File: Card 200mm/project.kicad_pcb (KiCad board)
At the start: 2 copper layers, 51.5 x 22 mm, 8 parts, among them J1 Conn_01x04, J2 Conn_01x10, J3 Conn_01x10, J4 Conn_01x10, J5 Conn_01x10, U1 24LC32, X0 Card Edge

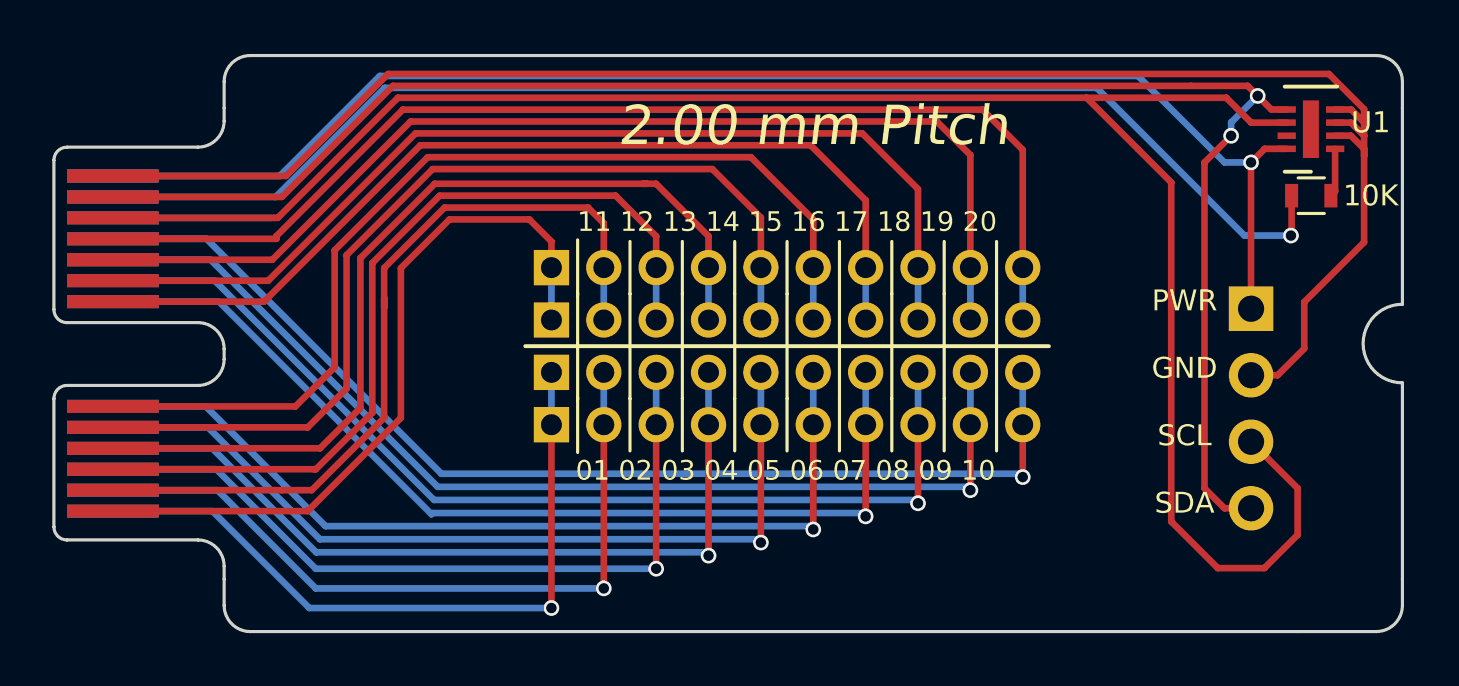
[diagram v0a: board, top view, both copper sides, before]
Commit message: EEPROM footprint update
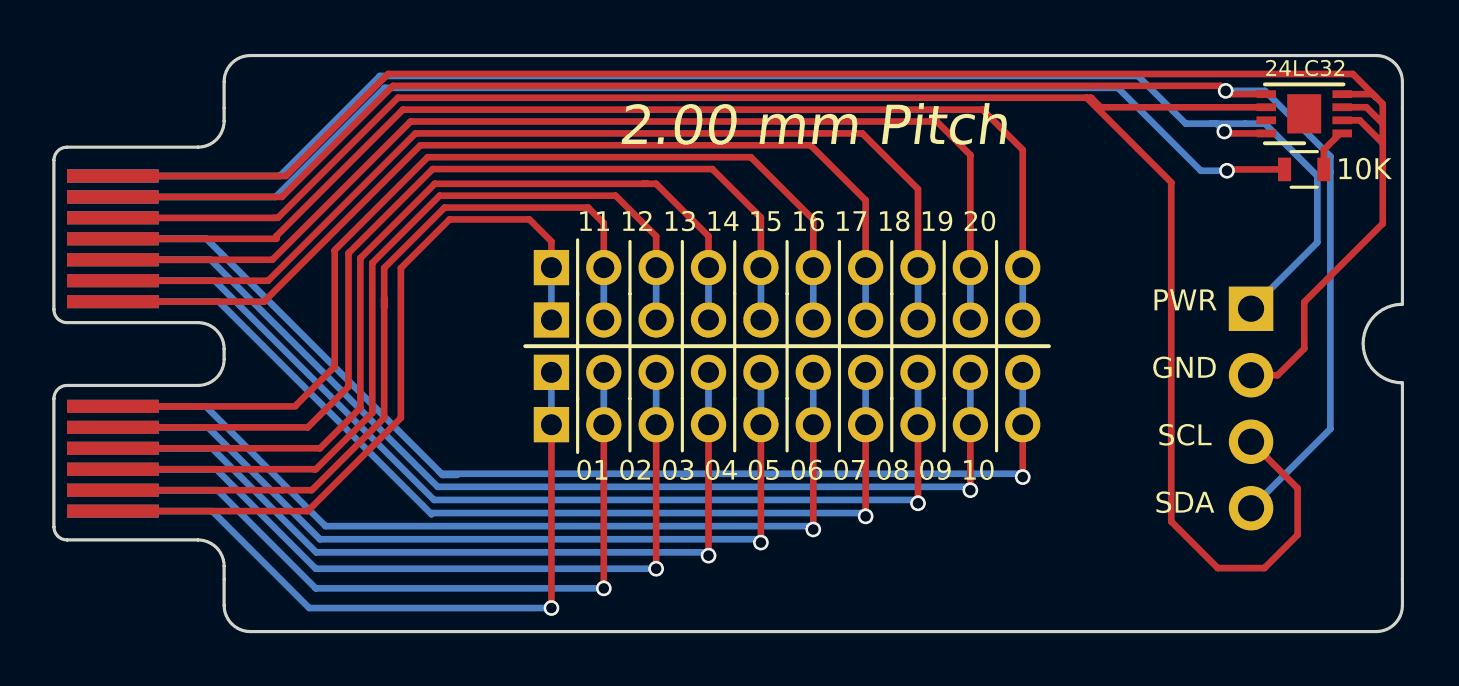
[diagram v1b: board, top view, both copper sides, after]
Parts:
- U1: footprint Package_DFN_QFN:DFN-8-1EP_2x3mm_P0.5mm_EP0.61x2.2mm -> footprints:DFN-8-1EP_3x2mm
- moved R1 1.04 mm to (47.8, -16.8)
- moved U1 0.64 mm to (47.8, -18.9)
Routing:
- net (no net): track 6.06 -> 0.00 mm
- net +5V: track 53.6 -> 57.5 mm
- net /A: track 50.6 -> 47.8 mm
- net GND: track 66.7 -> 68.7 mm
- net /D3_SCL: track 75.0 -> 74.0 mm
- net /D2_SDA: track 64.9 -> 65.7 mm, vias 2 -> 1
- net /10: track 42.5 -> 43.1 mm

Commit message: updates
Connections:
- J1 pad 1: +5V -> GND
- J1 pad 2: GND -> +5V
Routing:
- net +5V: track 57.5 -> 60.9 mm
- net GND: track 68.7 -> 66.6 mm
- net /10: track 43.1 -> 42.5 mm
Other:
- board text added: "2.00mm Pitch"
- board text added: "GND PWR SCL SDA"
- board text removed: "2.00 mm Pitch"
- board text removed: "PWR GND SCL SDA"

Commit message: Updates
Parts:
- moved U1 2.78 mm to (45.0, -18.5)
- moved R1 1.77 mm to (48.0, -18.5), turned to 90 degrees
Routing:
- net /D3_SCL: track 74.0 -> 59.2 mm
- net /D2_SDA: track 65.7 -> 74.2 mm
- net +5V: track 60.9 -> 56.3 mm
- net /A: track 47.8 -> 51.4 mm
- net GND: track 66.6 -> 64.1 mm
